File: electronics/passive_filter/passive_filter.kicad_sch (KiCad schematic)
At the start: 2 parts

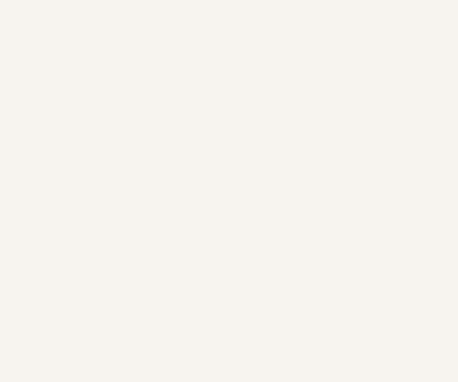
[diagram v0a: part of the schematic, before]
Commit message: completed passive filter
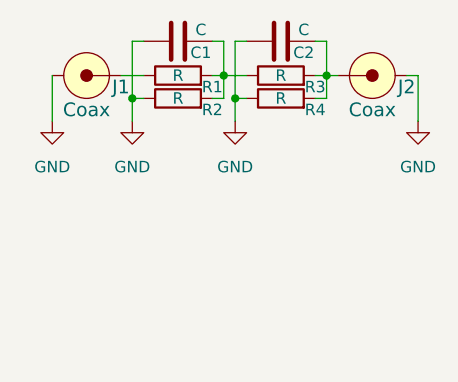
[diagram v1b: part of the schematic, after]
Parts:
- added C1, C2: C, SquantorCapacitor:C_0402+0603+0805+TH, symbol Device:C
- added J1, J2: Coax, SquantorConnectors:coax_edge_1.5_center_5_side, symbol SquantorConnectors:Coax
- added R1, R2, R3, R4: R, SquantorResistor:R_0805+0603, symbol Device:R
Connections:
- new net: C1.2, R1.2, R2.2, R3.1
- new net: C2.2, J2.1, R3.2, R4.2
- new net: J1.1, R1.1
- new net GND: C1.1, C2.1, J1.2, J2.2, R2.1, R4.1
